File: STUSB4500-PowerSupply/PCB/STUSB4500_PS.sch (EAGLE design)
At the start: 101 parts, among them J2 FEMALE 2x3, J3 FEMALE 2x3, J4 FEMALE 2x3, SW1 SPST_TACT-EVQQ2

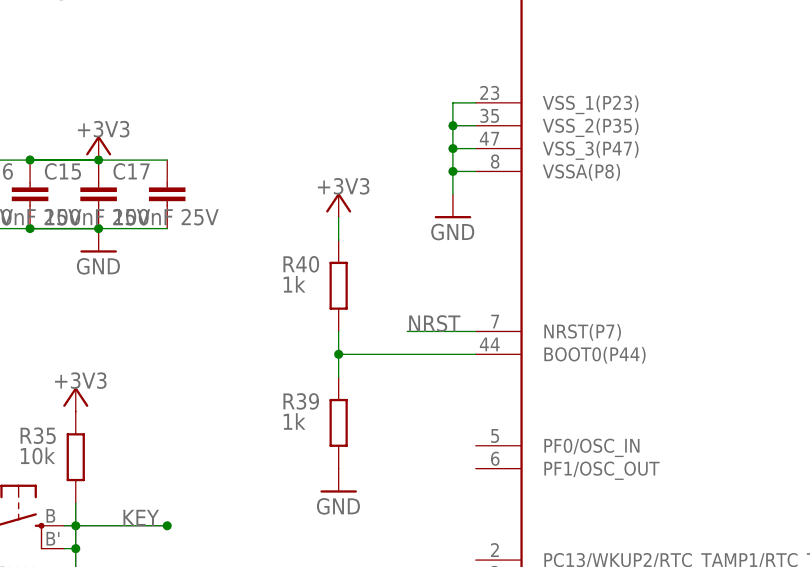
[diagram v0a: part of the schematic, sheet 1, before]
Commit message: Added reset pullup
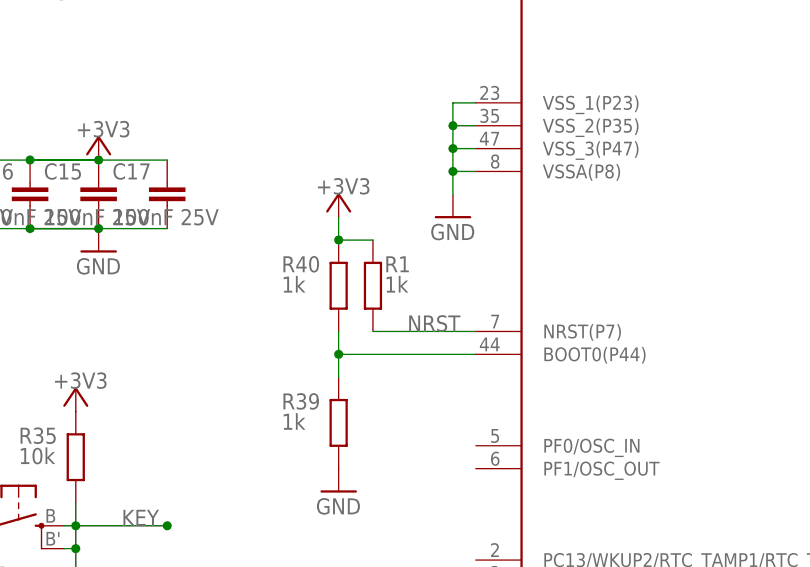
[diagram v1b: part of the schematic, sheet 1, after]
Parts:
- added R1: 1k, DD_rcl:R-EU_R0402
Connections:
- net +3V3: now also R1.2
- net NRST: now also R1.1
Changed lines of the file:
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@@
 <part name="P+4" library="supply1" library_urn="urn:adsk.eagle:library:371" deviceset="VCC" device="" value="DC-DC-5V0"/>
 <part name="P+5" library="supply1" library_urn="urn:adsk.eagle:library:371" deviceset="VCC" device="" value="DC-DC-3V3"/>
+<part name="R1" library="DD_rcl" deviceset="R-EU_" device="R0402" package3d_urn="urn:adsk.eagle:package:23547/3" value="1k"/>
 </parts>
 <sheets>
@@
 <attribute name="NAME" x="117.856" y="157.099" size="1.778" layer="95" rot="R180"/>
 <attribute name="VALUE" x="117.856" y="162.179" size="1.778" layer="96" rot="R180"/>
+</instance>
+<instance part="R1" gate="G$1" x="73.66" y="72.39" smashed="yes" rot="R90">
+<attribute name="NAME" x="74.93" y="73.8886" size="1.778" layer="95"/>
+<attribute name="VALUE" x="74.93" y="71.628" size="1.778" layer="96"/>
 </instance>
 </instances>
@@
 <pinref part="+3V15" gate="G$1" pin="+3V3"/>
 <wire x1="69.85" y1="77.47" x2="69.85" y2="80.01" width="0.1524" layer="91"/>
+<pinref part="R1" gate="G$1" pin="2"/>
+<wire x1="69.85" y1="77.47" x2="73.66" y2="77.47" width="0.1524" layer="91"/>
+<junction x="69.85" y="77.47"/>
 </segment>
 <segment>
@@
 <segment>
 <pinref part="U$8" gate="G$1" pin="NRST(P7)"/>
-<wire x1="85.09" y1="67.31" x2="77.47" y2="67.31" width="0.1524" layer="91"/>
+<wire x1="85.09" y1="67.31" x2="73.66" y2="67.31" width="0.1524" layer="91"/>
 <label x="77.47" y="67.31" size="1.778" layer="95"/>
-</segment>
-<segment>
+<pinref part="R1" gate="G$1" pin="1"/>
+</segment>
+<segment>

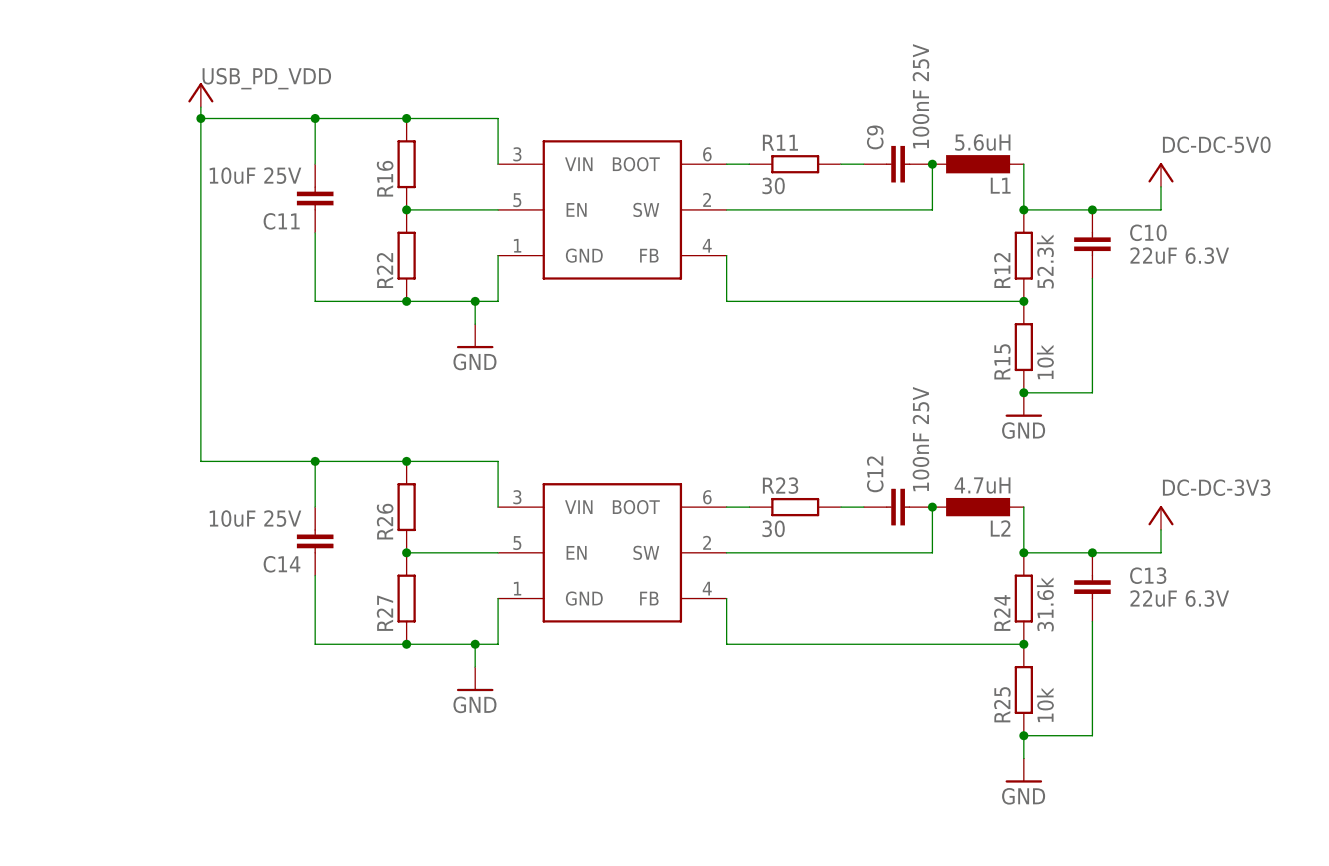
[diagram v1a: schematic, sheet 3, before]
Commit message: removed some unnecessary elements, added uc controlled dc-dc enable
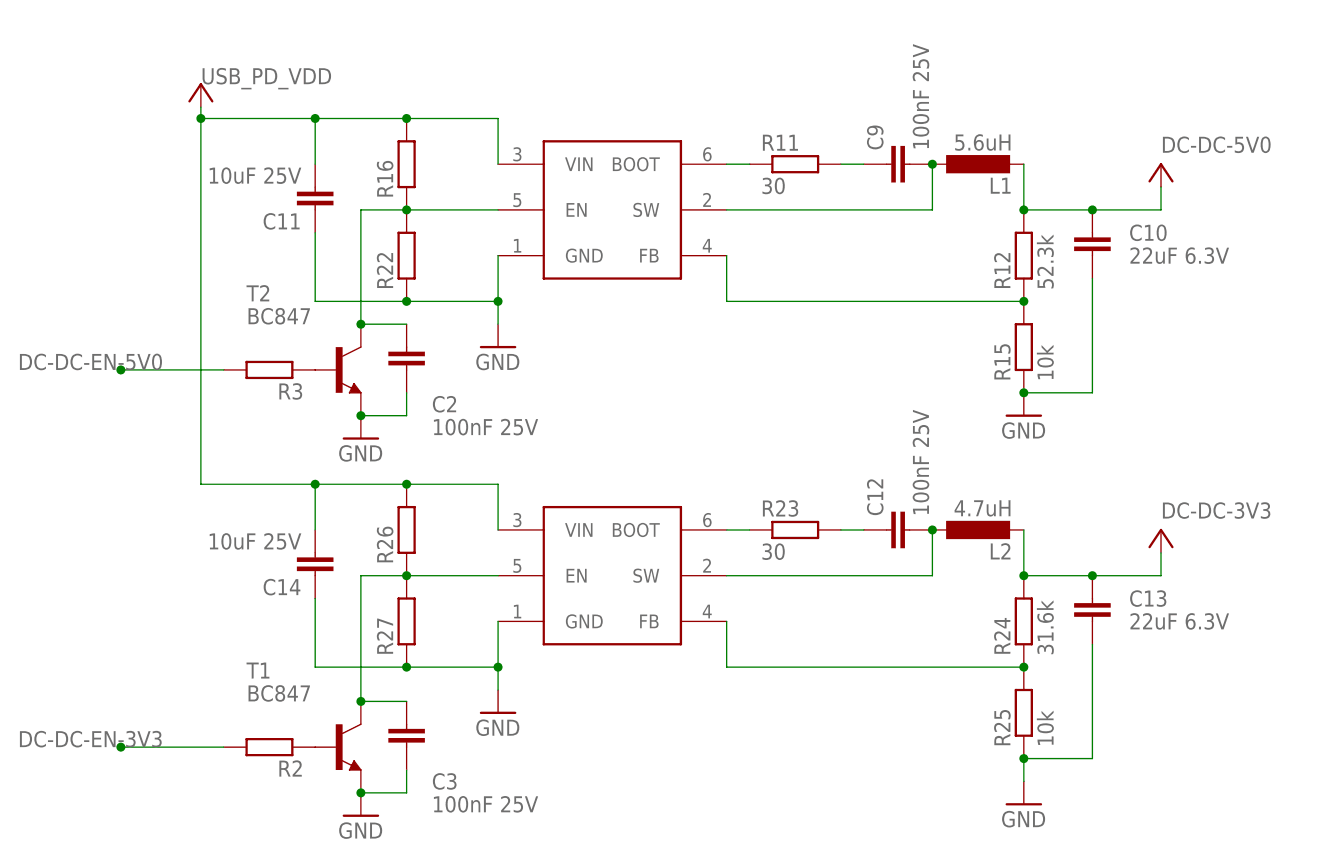
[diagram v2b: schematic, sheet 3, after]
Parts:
- removed LED2: GM1WA55311A, led:GM1WA55311A
- removed R13, R17, R18, R20, R21, R9: 1k, DD_rcl:R-EU_R0402
- removed R46, R47, R48: 22k, DD_rcl:R-EU_R0402
- added C2, C3: 100nF 25V, DD_rcl:C-EUC0402
- added R2, R3: (no value), DD_rcl:R-EU_R0402
- added T1, T2: BC847, transistor:BC847
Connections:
- removed net N$1: R17.1, U$9.A1
- removed net N$13: R20.2, U$10.A1
- removed net N$15: R21.2, U$10.A0
- removed net N$4: R18.1, U$9.A0
- removed net N$46: LED2.CGREEN, R46.2
- removed net N$47: LED2.CRED, R47.2
- removed net N$48: LED2.CBLUE, R48.2
- removed net N$8: R9.2, U$7.A1
- removed net N$9: R13.1, U$7.A0
- removed net STUSB_PDO2: R47.1, U$3.PDO2
- removed net STUSB_PDO3: R48.1, U$3.PDO3
- new net DC-DC-EN-3V3: R2.2, U$8.PB4/SPI1_MISO/TIM3_CH1
- new net DC-DC-EN-5V0: R3.2, U$8.PB3/SPI1_SCK/TIM2_CH2
- new net N$3: R2.1, T1.B
- new net N$5: R3.1, T2.B
- net +3V3: now also U$7.A0, U$9.A0, U$9.A1; no longer R13.2, R17.2, R18.2
- net GND: now also C2.1, C3.1, T1.E, T2.E, U$10.A0, U$10.A1, U$7.A1; no longer R20.1, R21.1, R46.1, R9.1
- net N$19: now also C2.2, T2.C
- net N$25: now also C3.2, T1.C
- net USB_PD_VDD: no longer LED2.A
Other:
- moved on the sheet: C12, C13, C14, L2, R23, R24, R25, R26, R27, R33, R34, R37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

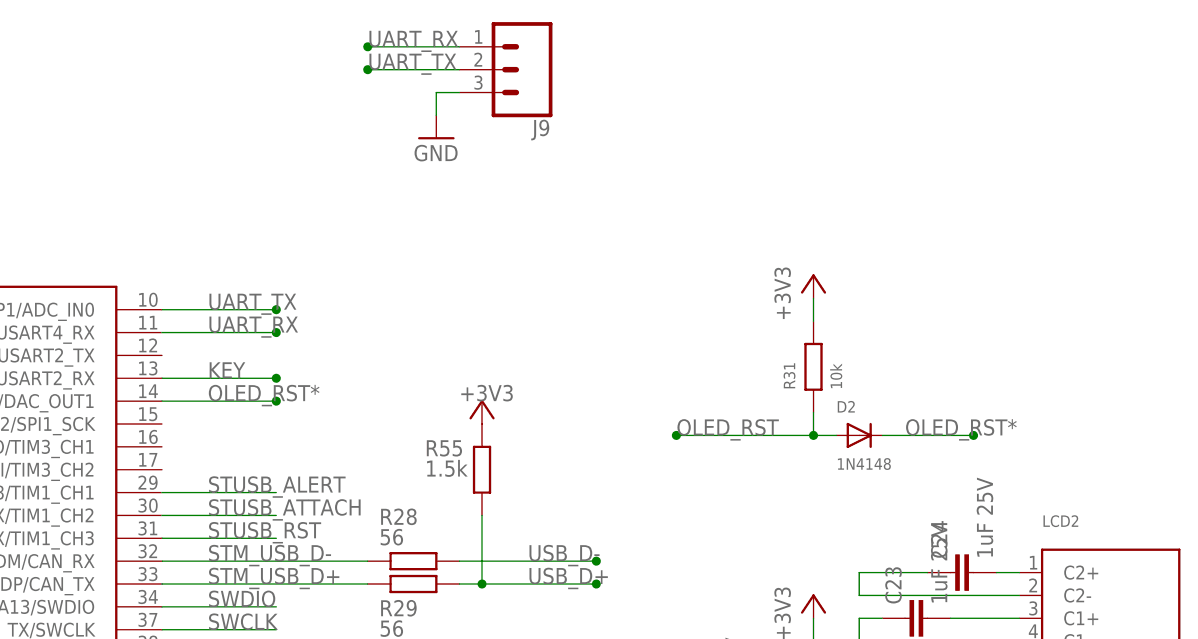
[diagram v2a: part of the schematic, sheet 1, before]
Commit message: Fixed OLED design, moved some lines
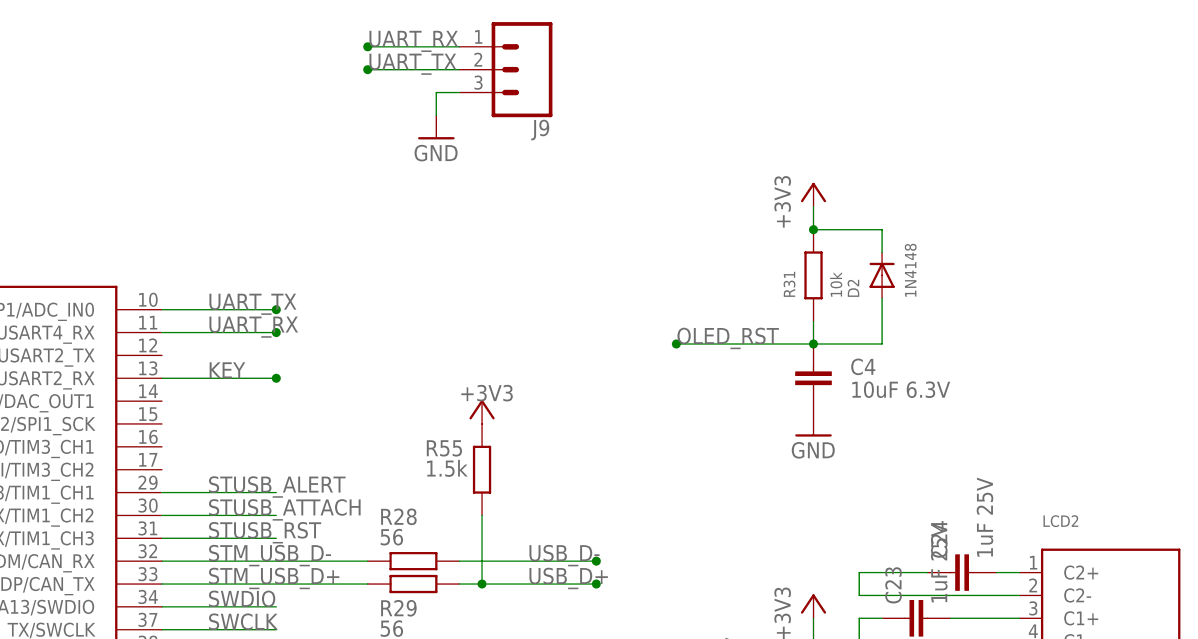
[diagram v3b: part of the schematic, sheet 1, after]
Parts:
- added C4: 10uF 6.3V, DD_rcl:C-EUC0603
- R31: device DD_rcl:R-EU_R0402 -> DD_rcl:R-EU_R0603
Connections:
- removed net OLED_RST*: D2.C, U$8.PA4/ADC_IN4/DAC_OUT1
- net +3V3: now also D2.C
- net GND: now also C4.1
- net OLED_RST: now also C4.2
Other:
- moved on the sheet: D2, R31

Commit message: Changed DC-DC coils to Wurth
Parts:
- L1, L2: device DD_rcl:L-EUPIS2816 -> DD_rcl:L-EUWE-TPC
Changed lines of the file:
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@@
 <part name="C11" library="DD_rcl" deviceset="C-EU" device="C1206" package3d_urn="urn:adsk.eagle:package:23618/2" value="10uF 25V"/>
 <part name="R22" library="DD_rcl" deviceset="R-EU_" device="R0402" package3d_urn="urn:adsk.eagle:package:23547/3"/>
-<part name="L1" library="DD_rcl" deviceset="L-EU" device="PIS2816" package3d_urn="urn:adsk.eagle:package:23515/1" value="5.6uH"/>
+<part name="L1" library="DD_rcl" deviceset="L-EU" device="WE-TPC" package3d_urn="urn:adsk.eagle:package:25966/1" value="5.6uH"/>
 <part name="U$12" library="DD_TPS56339" deviceset="TPS56339" device="SOT23-6" package3d_urn="urn:adsk.eagle:package:15662283/2"/>
 <part name="GND30" library="supply1" library_urn="urn:adsk.eagle:library:371" deviceset="GND" device=""/>
@@
 <part name="C14" library="DD_rcl" deviceset="C-EU" device="C1206" package3d_urn="urn:adsk.eagle:package:23618/2" value="10uF 25V"/>
 <part name="R27" library="DD_rcl" deviceset="R-EU_" device="R0402" package3d_urn="urn:adsk.eagle:package:23547/3"/>
-<part name="L2" library="DD_rcl" deviceset="L-EU" device="PIS2816" package3d_urn="urn:adsk.eagle:package:23515/1" value="4.7uH"/>
+<part name="L2" library="DD_rcl" deviceset="L-EU" device="WE-TPC" package3d_urn="urn:adsk.eagle:package:25966/1" value="4.7uH"/>
 <part name="LCD2" library="DD_microbuilder" deviceset="DISP_OLED_UG-2832HSWEG02" device=""/>
 <part name="R30" library="DD_rcl" deviceset="R-EU_" device="R0603" package3d_urn="urn:adsk.eagle:package:23555/3" value="390K"/>
